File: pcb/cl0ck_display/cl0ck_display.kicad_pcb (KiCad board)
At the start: 2 copper layers, 307 x 27 mm, 16 parts, among them P1 CONN_01X03, P2 CONN_01X02

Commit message: Revision to pcbs.
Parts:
- moved P2 1.20 mm to (203.5, 135.5)
- moved P1 0.10 mm to (203.5, 140.5)
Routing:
- net VCC: track 183.8 -> 185.2 mm, vias 8 -> 4

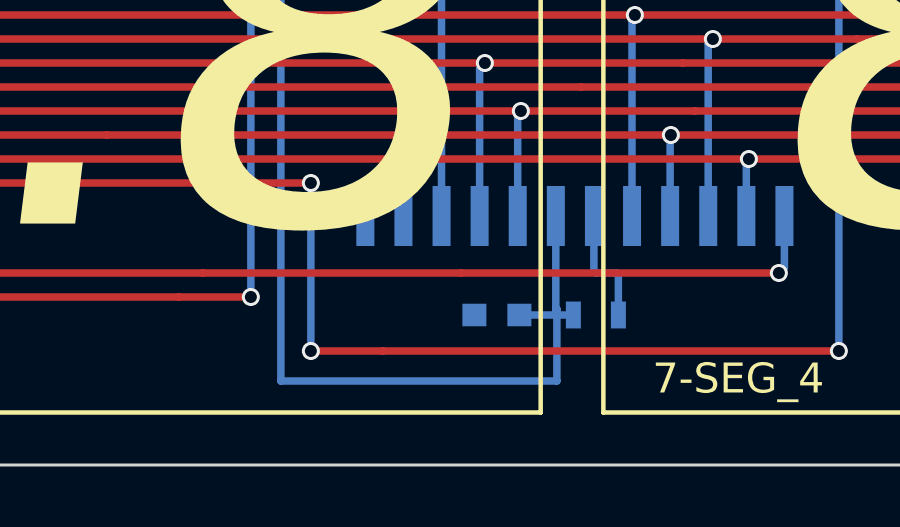
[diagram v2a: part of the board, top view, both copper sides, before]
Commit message: Prototype display board PCB fabricated.  One error found - decoupling capacitor not grounded.  Iterated pcb layout to remedy (added via).
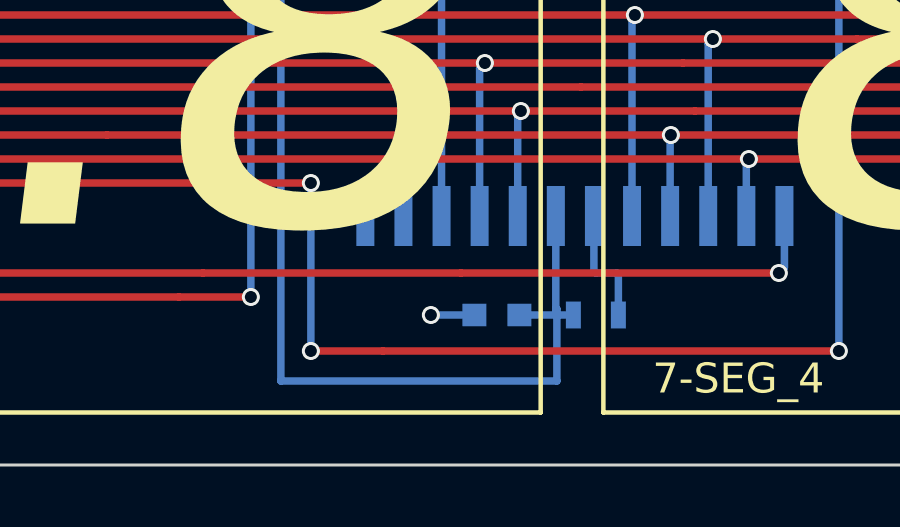
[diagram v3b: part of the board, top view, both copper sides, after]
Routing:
- net GND: track 0.00 -> 1.45 mm, vias 0 -> 1
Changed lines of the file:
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@@
   (general
     (links 68)
-    (no_connects 1)
+    (no_connects 0)
     (area 49.949999 126.949999 357.050001 154.050001)
     (thickness 1.6)
     (drawings 16)
-    (tracks 486)
+    (tracks 488)
     (zones 0)
     (modules 16)
@@
   (segment (start 131.4 149) (end 131.85 149) (width 0.25) (layer B.Cu) (net 17))
   (segment (start 131.365 148.965) (end 131.4 149) (width 0.25) (layer B.Cu) (net 17))
+  (segment (start 271.85 149) (end 270.4 149) (width 0.25) (layer B.Cu) (net 18) (status 400000))
+  (via (at 270.4 149) (size 0.6) (drill 0.4) (layers F.Cu B.Cu) (net 18))
   (segment (start 125.015 136.3) (end 125.015 130.585) (width 0.25) (layer B.Cu) (net 19))
   (segment (start 200 140.4) (end 203.5 140.4) (width 0.25) (layer B.Cu) (net 19))
